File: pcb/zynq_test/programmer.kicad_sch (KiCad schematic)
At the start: 42 parts, among them J601 USB_B_Micro, J602 Conn_01x06_Pin, U601 FT2232HQ, U602 93LCxxB, U603 DSC1001CI2-012, U604 ESD8104, U605 ESD8104

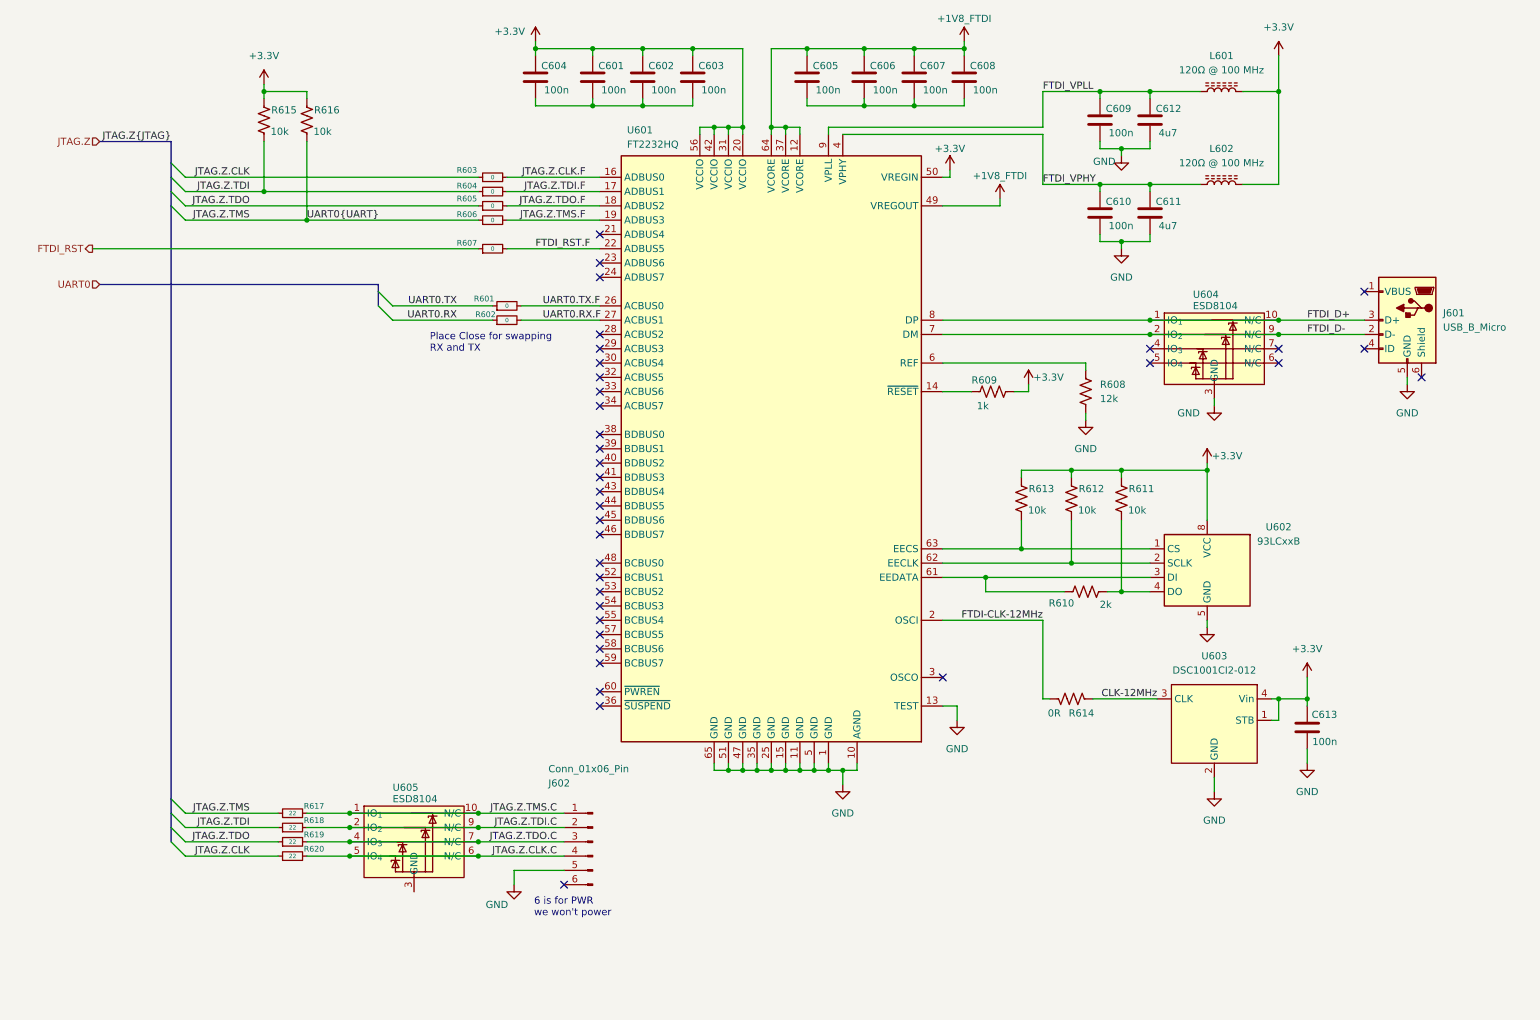
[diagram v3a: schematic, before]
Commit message: Connected DDR3, cleaned up some thing
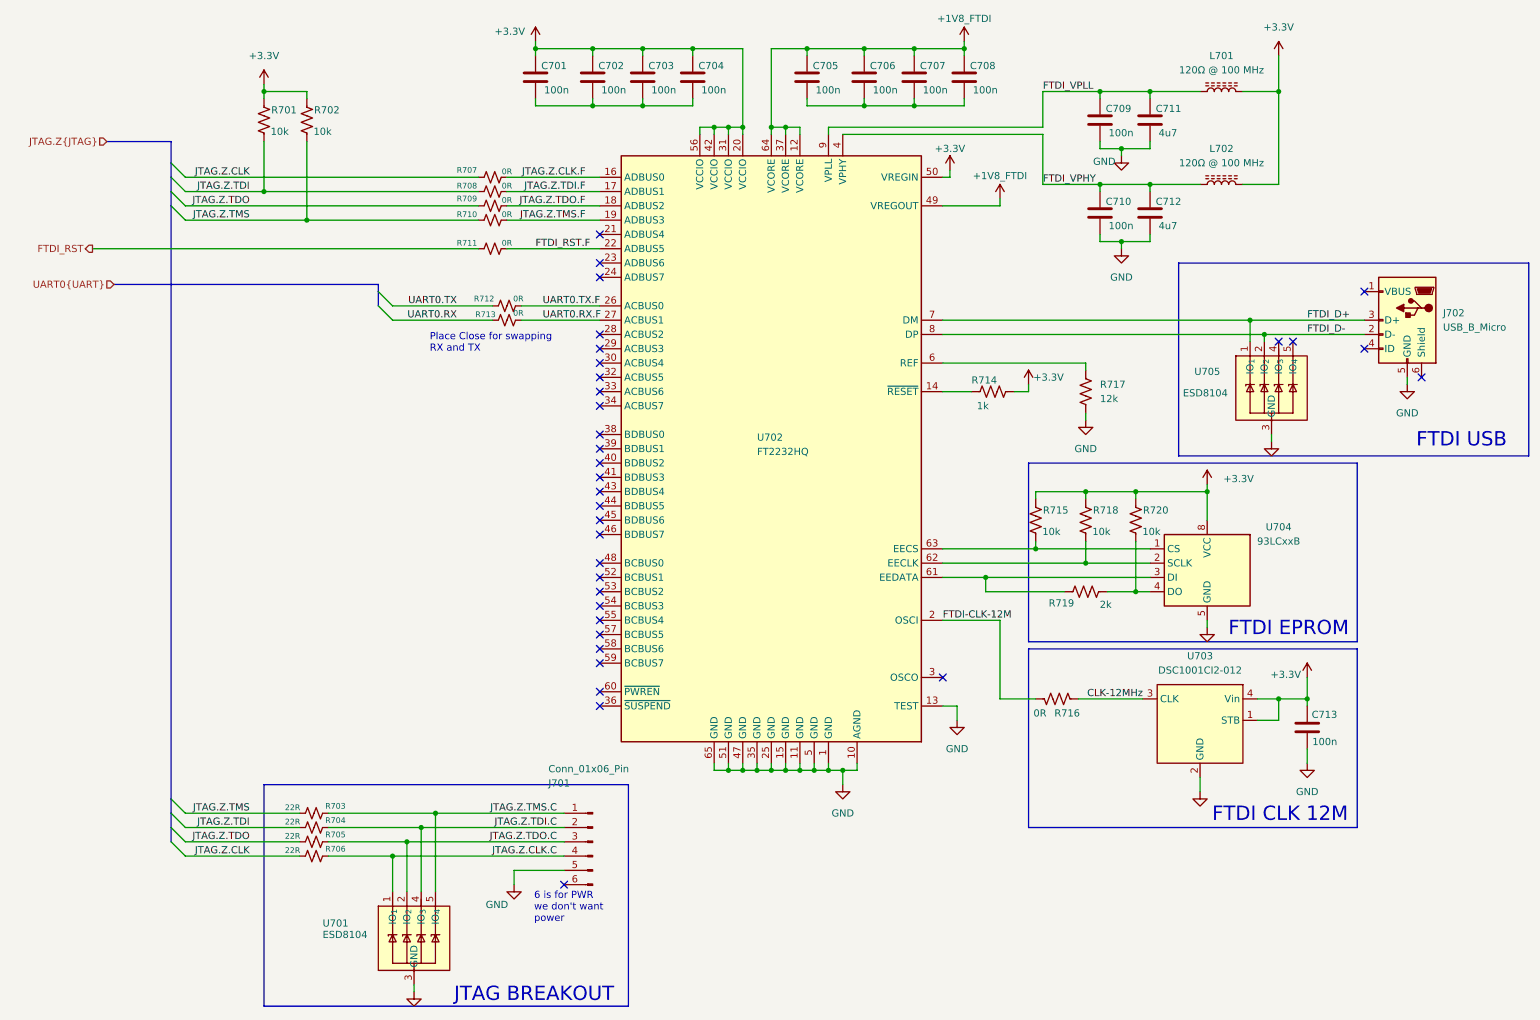
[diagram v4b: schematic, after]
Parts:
- J702: renamed from J601; footprint (none) -> Connector_USB:USB_Micro-B_Amphenol_10118193-0001LF_Horizontal
- R703: renamed from R617; value 22 -> 22R; symbol Device:R_Small -> Device:R_Small_US
- R704: renamed from R618; value 22 -> 22R; symbol Device:R_Small -> Device:R_Small_US
- R705: renamed from R619; value 22 -> 22R; symbol Device:R_Small -> Device:R_Small_US
- R706: renamed from R620; value 22 -> 22R; symbol Device:R_Small -> Device:R_Small_US
- R707: renamed from R603; value 0 -> 0R; symbol Device:R_Small -> Device:R_Small_US
- R708: renamed from R604; value 0 -> 0R; symbol Device:R_Small -> Device:R_Small_US
- R709: renamed from R605; value 0 -> 0R; symbol Device:R_Small -> Device:R_Small_US
- R710: renamed from R606; value 0 -> 0R; symbol Device:R_Small -> Device:R_Small_US
- R711: renamed from R607; value 0 -> 0R; symbol Device:R_Small -> Device:R_Small_US
- R712: renamed from R601; value 0 -> 0R; symbol Device:R_Small -> Device:R_Small_US
- R713: renamed from R602; value 0 -> 0R; symbol Device:R_Small -> Device:R_Small_US
- renumbered C604 to C701, C601 to C702, C602 to C703, C603 to C704, C605 to C705, C606 to C706, C607 to C707, C608 to C708, C609 to C709, C610 to C710, C612 to C711, C611 to C712, C613 to C713, J602 to J701, L601 to L701, L602 to L702, R615 to R701, R616 to R702, R609 to R714, R613 to R715, R614 to R716, R608 to R717, R612 to R718, R610 to R719, R611 to R720, U605 to U701, U601 to U702, U603 to U703, U602 to U704, U604 to U705
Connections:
- net FTDI_D+: now also U702.7 (DM); no longer U702.8 (DP)
- net FTDI_D-: now also U702.8 (DP); no longer U702.7 (DM)
- net GND: now also U701.3 (GND), U701.8 (GND), U705.8 (GND)
- net JTAG.Z.CLK.C: now also U701.1 (IO_{1}), U701.10 (N/C); no longer U701.5 (IO_{4}), U701.6 (N/C)
- net JTAG.Z.TDI.C: now also U701.4 (IO_{3}), U701.7 (N/C); no longer U701.2 (IO_{2}), U701.9 (N/C)
- net JTAG.Z.TDO.C: now also U701.2 (IO_{2}), U701.9 (N/C); no longer U701.4 (IO_{3}), U701.7 (N/C)
- net JTAG.Z.TMS.C: now also U701.5 (IO_{4}), U701.6 (N/C); no longer U701.1 (IO_{1}), U701.10 (N/C)
- net at U705.4 (IO_{3}): now also U705.7 (N/C)
- net at U705.5 (IO_{4}): now also U705.6 (N/C)
- net FTDI-CLK-12MHz renamed FTDI-CLK-12M
- no-connect marks 36 -> 34
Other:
- note added: "6 is for PWR we don't want power"
- note added: "FTDI CLK 12M"
- note added: "FTDI EPROM"
- note added: "FTDI USB"
- note added: "JTAG BREAKOUT"
- note removed: "6 is for PWR we won't power"
- moved on the sheet: R715, R716, R718, R720, U703

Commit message: Finished Power Supply
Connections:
- net +3.3V renamed +3V3
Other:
- title: (none) -> JTAG Proggrammer
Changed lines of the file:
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@@
 	(paper "A4")
 	(title_block
-		(date "2025-09-06")
-		(rev "v1.0")
+		(title "JTAG Proggrammer")
+		(date "2025-09-13")
+		(rev "A")
 	)
 	(rectangle
@@
 			)
 		)
-		(property "Value" "+3.3V"
+		(property "Value" "+3V3"
 			(at 194.056 82.55 0)
 			(effects
@@
 			)
 		)
-		(property "Value" "+3.3V"
+		(property "Value" "+3V3"
 			(at 227.838 100.584 0)
 			(effects
@@
 			)
 		)
-		(property "Value" "+3.3V"
+		(property "Value" "+3V3"
 			(at 234.95 20.32 0)
 			(effects
@@
 			)
 		)
-		(property "Value" "+3.3V"
+		(property "Value" "+3V3"
 			(at 98.298 21.082 0)
 			(effects
@@
 			)
 		)
-		(property "Value" "+3.3V"
+		(property "Value" "+3V3"
 			(at 236.22 135.382 0)
 			(effects
@@
 			)
 		)
-		(property "Value" "+3.3V"
+		(property "Value" "+3V3"
 			(at 54.61 25.4 0)
 			(effects
@@
 			)
 		)
-		(property "Value" "+3.3V"
+		(property "Value" "+3V3"
 			(at 176.53 41.91 0)
 			(effects

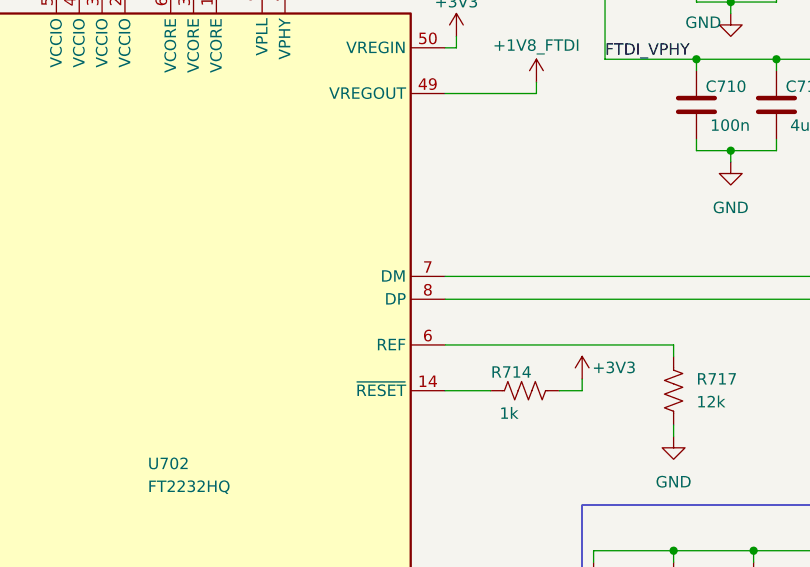
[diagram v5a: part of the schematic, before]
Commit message: Finished most of the schematic, will start routing soon
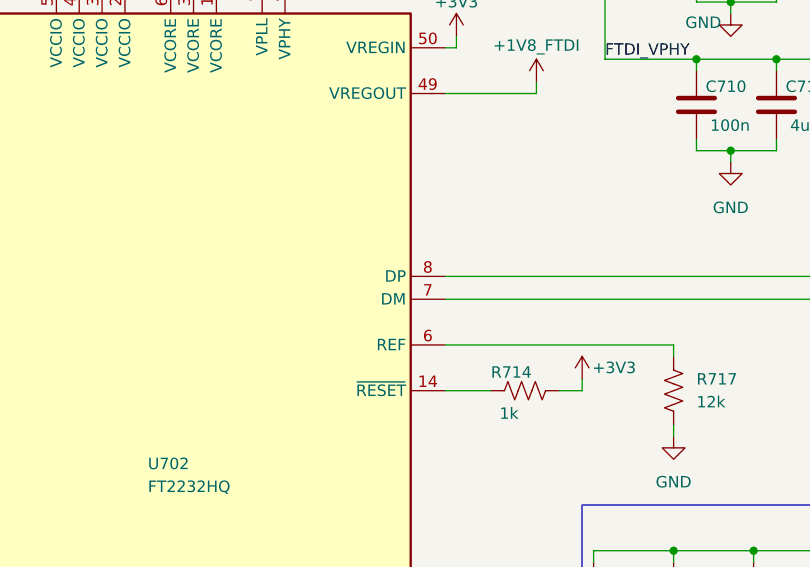
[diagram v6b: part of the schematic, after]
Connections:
- net FTDI_D+: now also U702.8 (DP); no longer U702.7 (DM)
- net FTDI_D-: now also U702.7 (DM); no longer U702.8 (DP)

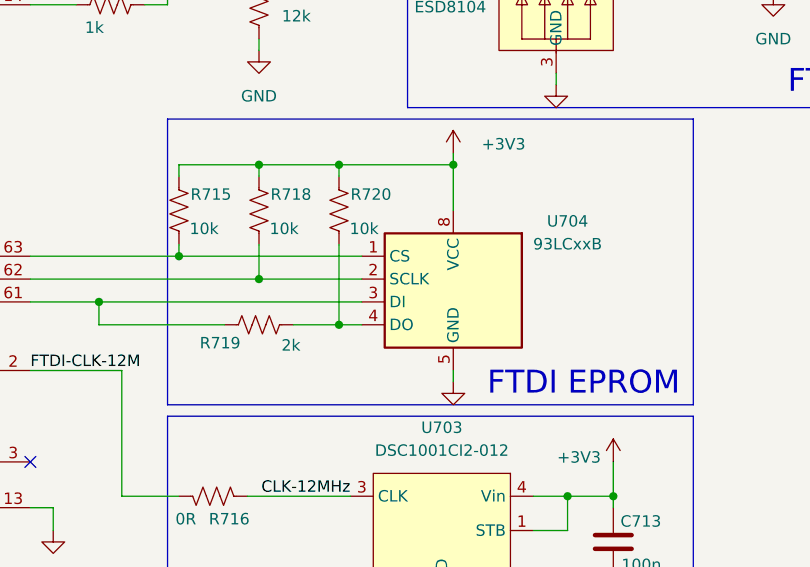
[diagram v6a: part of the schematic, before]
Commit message: finished diff of HDMI
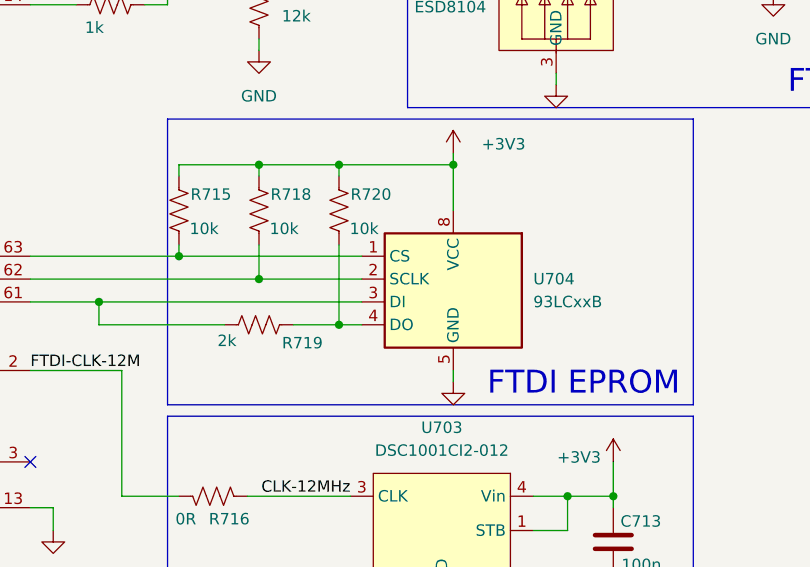
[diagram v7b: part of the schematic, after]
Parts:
- J701: footprint (none) -> Connector_PinHeader_2.54mm:PinHeader_1x06_P2.54mm_Vertical
- R701, R702, R703, R704, R705, R706, R707, R708, R709, R710, R711, R712, R713, R714, R716, R717: footprint (none) -> Resistor_SMD:R_0402_1005Metric
- U701, U705: footprint (none) -> Package_DFN_QFN:Diodes_UDFN-10_1.0x2.5mm_P0.5mm
- U703: footprint (none) -> other:DSC1001
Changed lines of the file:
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@@
 		(dnp no)
 		(property "Reference" "R719"
-			(at 196.342 122.682 90)
+			(at 205.486 122.682 90)
 			(effects
 				(font
@@
 		)
 		(property "Value" "2k"
-			(at 204.216 122.936 90)
+			(at 197.104 122.428 90)
 			(effects
 				(font
@@
 			)
 		)
-		(property "Footprint" ""
+		(property "Footprint" "Resistor_SMD:R_0402_1005Metric"
 			(at 63.5 165.1 0)
 			(effects
@@
 			)
 		)
-		(property "Footprint" ""
+		(property "Footprint" "Resistor_SMD:R_0402_1005Metric"
 			(at 97.79 69.85 0)
 			(effects
@@
 			)
 		)
-		(property "Footprint" ""
+		(property "Footprint" "Resistor_SMD:R_0402_1005Metric"
 			(at 195.326 138.684 90)
 			(effects
@@
 			)
 		)
-		(property "Footprint" ""
+		(property "Footprint" "Package_DFN_QFN:Diodes_UDFN-10_1.0x2.5mm_P0.5mm"
 			(at 233.68 80.01 0)
 			(effects
@@
 			)
 		)
-		(property "Footprint" ""
+		(property "Footprint" "Resistor_SMD:R_0402_1005Metric"
 			(at 95.25 52.07 0)
 			(effects
@@
 			)
 		)
-		(property "Footprint" ""
+		(property "Footprint" "Resistor_SMD:R_0402_1005Metric"
 			(at 201.676 85.344 90)
 			(effects
@@
 			)
 		)
-		(property "Footprint" ""
+		(property "Footprint" "Resistor_SMD:R_0402_1005Metric"
 			(at 97.79 72.39 0)
 			(effects
@@
 			)
 		)
-		(property "Footprint" ""
+		(property "Footprint" "Resistor_SMD:R_0402_1005Metric"
 			(at 95.25 49.53 0)
 			(effects
@@
 			)
 		)
-		(property "Footprint" ""
+		(property "Footprint" "other:DSC1001"
 			(at 220.98 143.51 0)
 			(effects
@@
 			)
 		)
-		(property "Footprint" ""
+		(property "Footprint" "Resistor_SMD:R_0402_1005Metric"
 			(at 53.594 36.576 90)
 			(effects
@@
 			)
 		)
-		(property "Footprint" ""
+		(property "Footprint" "Resistor_SMD:R_0402_1005Metric"
 			(at 63.5 160.02 0)
 			(effects
@@
 			)
 		)
-		(property "Footprint" ""
+		(property "Footprint" "Resistor_SMD:R_0402_1005Metric"
 			(at 61.214 36.576 90)
 			(effects
@@
 			)
 		)
-		(property "Footprint" ""
+		(property "Footprint" "Resistor_SMD:R_0402_1005Metric"
 			(at 184.404 84.074 90)
 			(effects
@@
 		(fields_autoplaced yes)
 		(property "Reference" "U704"
-			(at 234.95 109.1498 0)
+			(at 231.14 115.5699 0)
 			(effects
 				(font
 					(size 1.27 1.27)
 				)
+				(justify right)
 			)
 		)
 		(property "Value" "93LCxxB"
-			(at 234.95 111.6898 0)
+			(at 231.14 118.1099 0)
 			(effects
 				(font
 					(size 1.27 1.27)
 				)
+				(justify right)
 			)
 		)
@@
 			)
 		)
-		(property "Footprint" ""
+		(property "Footprint" "Resistor_SMD:R_0402_1005Metric"
 			(at 95.25 54.61 0)
 			(effects
@@
 			)
 		)
-		(property "Footprint" ""
+		(property "Footprint" "Connector_PinHeader_2.54mm:PinHeader_1x06_P2.54mm_Vertical"
 			(at 113.03 165.1 0)
 			(effects
@@
 			)
 		)
-		(property "Footprint" ""
+		(property "Footprint" "Resistor_SMD:R_0402_1005Metric"
 			(at 63.5 162.56 0)
 			(effects
@@
 			)
 		)
-		(property "Footprint" ""
+		(property "Footprint" "Resistor_SMD:R_0402_1005Metric"
 			(at 95.25 46.99 0)
 			(effects
@@
 			)
 		)
-		(property "Footprint" ""
+		(property "Footprint" "Package_DFN_QFN:Diodes_UDFN-10_1.0x2.5mm_P0.5mm"
 			(at 81.28 177.8 0)
 			(effects
@@
 			)
 		)
-		(property "Footprint" ""
+		(property "Footprint" "Resistor_SMD:R_0402_1005Metric"
 			(at 63.5 167.64 0)
 			(effects
@@
 			)
 		)
-		(property "Footprint" ""
+		(property "Footprint" "Resistor_SMD:R_0402_1005Metric"
 			(at 95.25 59.69 0)
 			(effects

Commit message: Almost done with BOM
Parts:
- added U706: 74AUC1G07, Package_TO_SOT_SMD:SOT-23-5, symbol 74xGxx:74AUC1G07
- C701, C702, C703, C704, C705, C706, C707, C708, C709, C710, C711, C712, C713: footprint (none) -> Capacitor_SMD:C_0402_1005Metric
- L701, L702: footprint (none) -> Capacitor_SMD:C_0603_1608Metric
- R715, R718, R719, R720: footprint (none) -> Resistor_SMD:R_0402_1005Metric
- U704: footprint (none) -> Package_SO:SOIC-8_3.9x4.9mm_P1.27mm
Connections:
- net +3V3: now also U702.21 (ADBUS4), U706.5 (VCC)
- net GND: now also C701.2, C702.2, C703.2, C704.2, C705.2, C706.2, C707.2, C708.2, U706.3 (GND)
- net FTDI_POR_B: now reaches U702.23 (ADBUS6)
- net FTDI_POR_B: now also U706.2
- net FTDI_RST renamed POR_B
- net FTDI_RST.F: no longer names the net of R711.2
- net FTDI_RST.F: now also U706.4; no longer U702.22 (ADBUS5)
- no-connect marks 34 -> 33
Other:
- moved on the sheet: R711
